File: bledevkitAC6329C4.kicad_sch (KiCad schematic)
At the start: 32 parts, among them J1 USB_C_Receptacle_USB2.0_16P, J2 Conn_01x02, J4 Conn_01x07, J5 Qwiic_I2C_connector, J6 Conn_01x07, J7 Conn_01x02, J8 Conn_01x01, SW1 SW_DPDT_x2, SW2 SW_DPDT_x2, SW3 SW_Push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

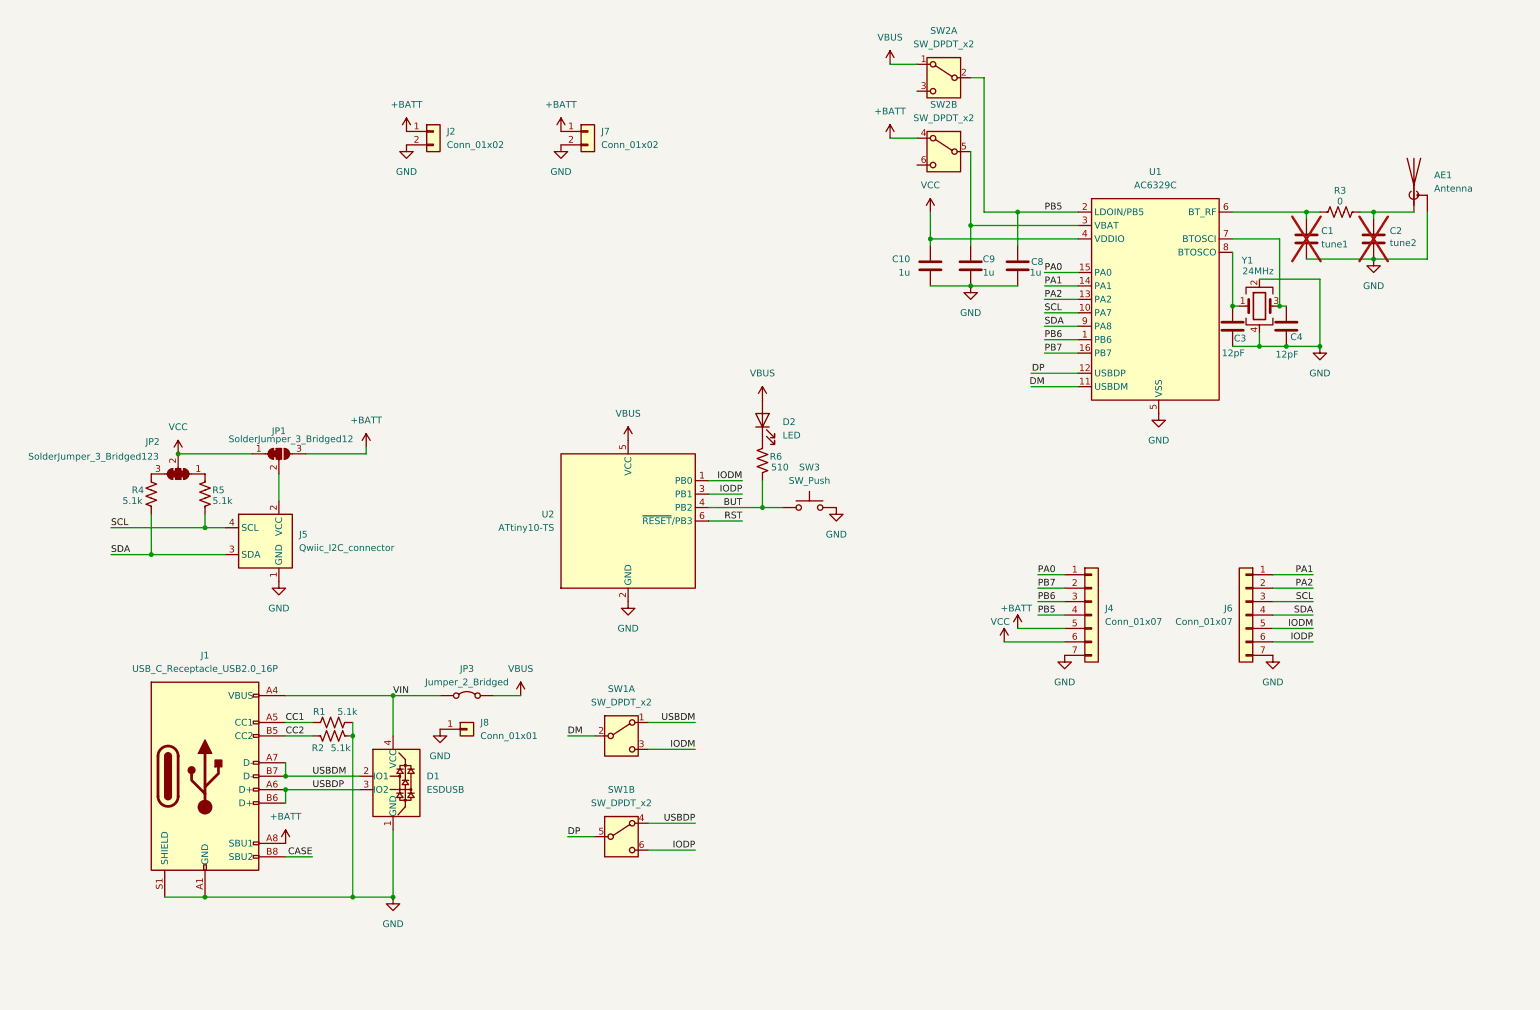
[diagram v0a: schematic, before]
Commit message: Finalized power topology
Isolated all power draws other than AC6329 behind current probe point.  Added auxiliary 3.3V regulator as an option for Qwiic header.  Shouldn't need any schematic changes, just on to making things fit and adding the switch footprints.
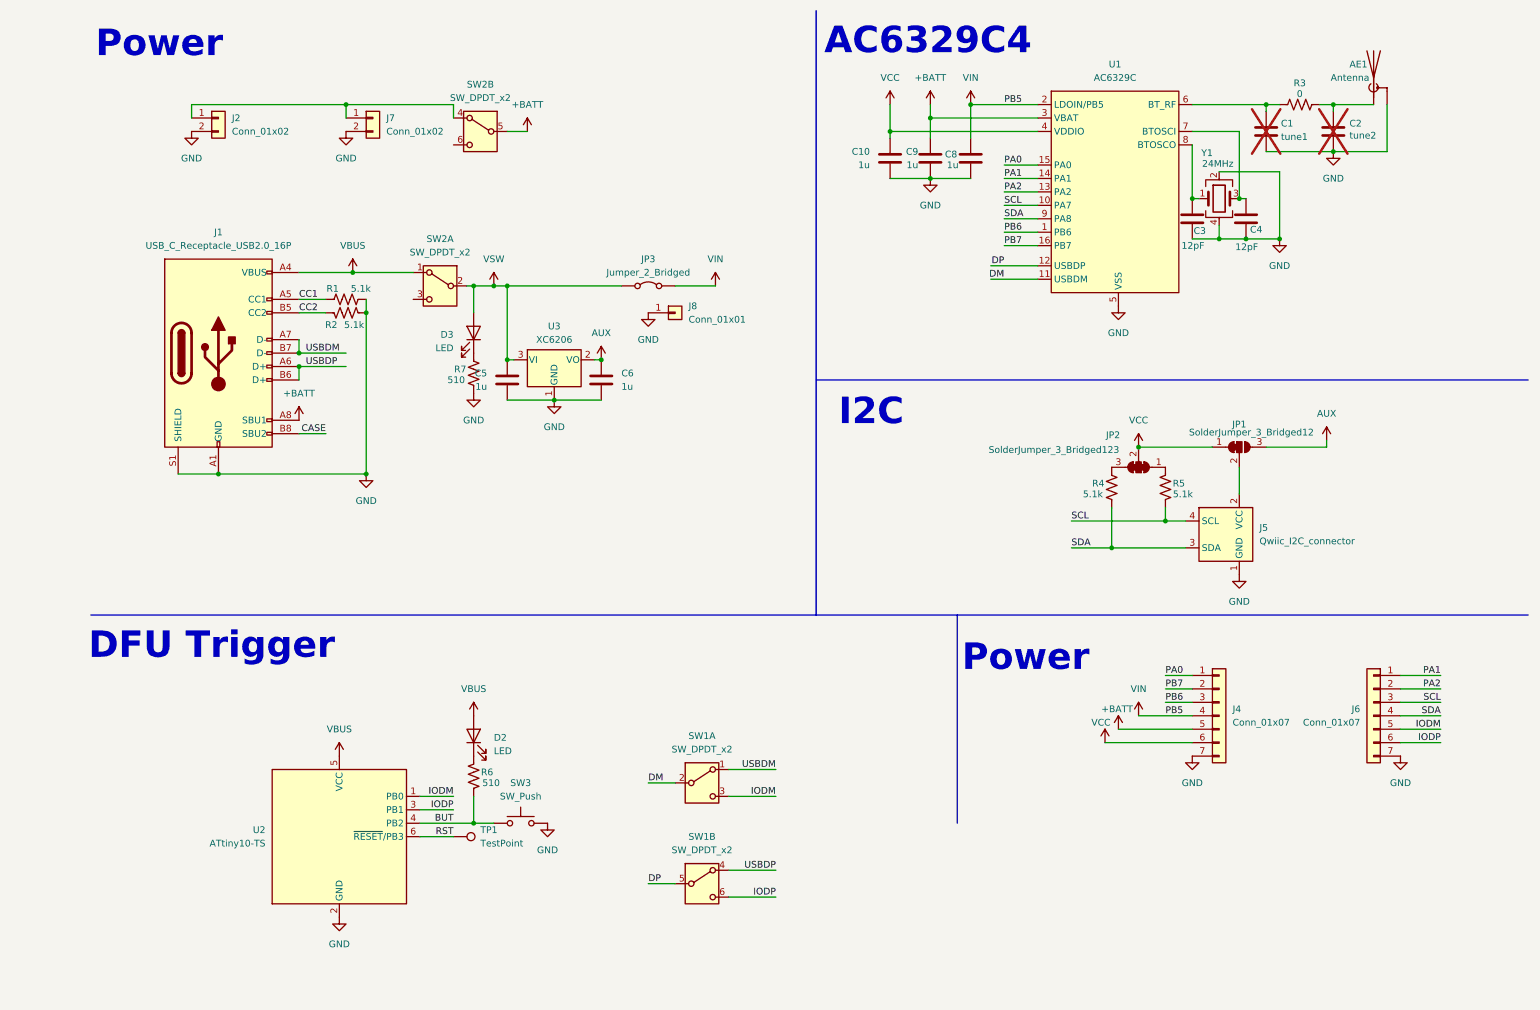
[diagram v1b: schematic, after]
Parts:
- removed D1: ESDUSB, Package_TO_SOT_SMD:SOT-143, symbol maxkicad:ESDUSB
- added C5, C6: 1u, Capacitor_SMD:C_0402_1005Metric, symbol Device:C
- added D3: LED, LED_SMD:LED_0402_1005Metric, symbol Device:LED
- added R7: 510, Resistor_SMD:R_0402_1005Metric, symbol Device:R_US
- added TP1: TestPoint, TestPoint:TestPoint_Pad_D3.0mm, symbol Connector:TestPoint
- added U3: XC6206, Package_TO_SOT_SMD:SOT-23-3, symbol Regulator_Linear:XC6206PxxxMR
- J5: footprint Connector_JST:JST_SH_BM04B-SRSS-TB_1x04-1MP_P1.00mm_Vertical -> Connector_JST:JST_SH_SM04B-SRSS-TB_1x04-1MP_P1.00mm_Horizontal
- J8: footprint Connector_PinSocket_2.54mm:PinSocket_1x01_P2.54mm_Vertical -> Connector_PinHeader_2.54mm:PinHeader_1x01_P2.54mm_Vertical
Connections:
- net +BATT: now also C9.1, SW2.5 (B), U1.3 (VBAT); no longer J2.1 (Pin_1), J7.1 (Pin_1), JP1.3 (B), SW2.4 (A)
- net GND: now also C5.2, C6.2, R7.1, U3.1 (GND)
- net RST: now also TP1.1
- net VBUS: now also J1.A4 (VBUS), J1.A9 (VBUS), J1.B4 (VBUS), J1.B9 (VBUS); no longer JP3.2 (B)
- net VIN: now also C8.1, J4.4 (Pin_4), JP3.2 (B), U1.2 (LDOIN/PB5); no longer J1.A4 (VBUS), J1.A9 (VBUS), J1.B4 (VBUS), J1.B9 (VBUS), JP3.1 (A)
- removed net PB5: C8.1, J4.4 (Pin_4), SW2.2 (B), U1.2 (LDOIN/PB5)
- new net: J2.1 (Pin_1), J7.1 (Pin_1), SW2.4 (A)
- new net: D3.1 (K), R7.2
- new net AUX: C6.1, JP1.3 (B), U3.2 (VO)
- new net VSW: C5.1, D3.2 (A), JP3.1 (A), SW2.2 (B), U3.3 (VI)
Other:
- note added: "AC6329C4"
- note added: "DFU Trigger"
- note added: "I2C"
- note added: "Power"
- moved on the sheet: AE1, C1, C10, C2, C3, C4, C8, C9, D2, J1, J2, J4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

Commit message: Finalized switches, chose modern DFU trigger
Switched to the newest series of the ATTINY line for UPDI programming, which can be done over the USB-C connector for simplicity of flashing.  Also made custom footprints for SMD DPDT slide switches.  Temp routing 80% done.
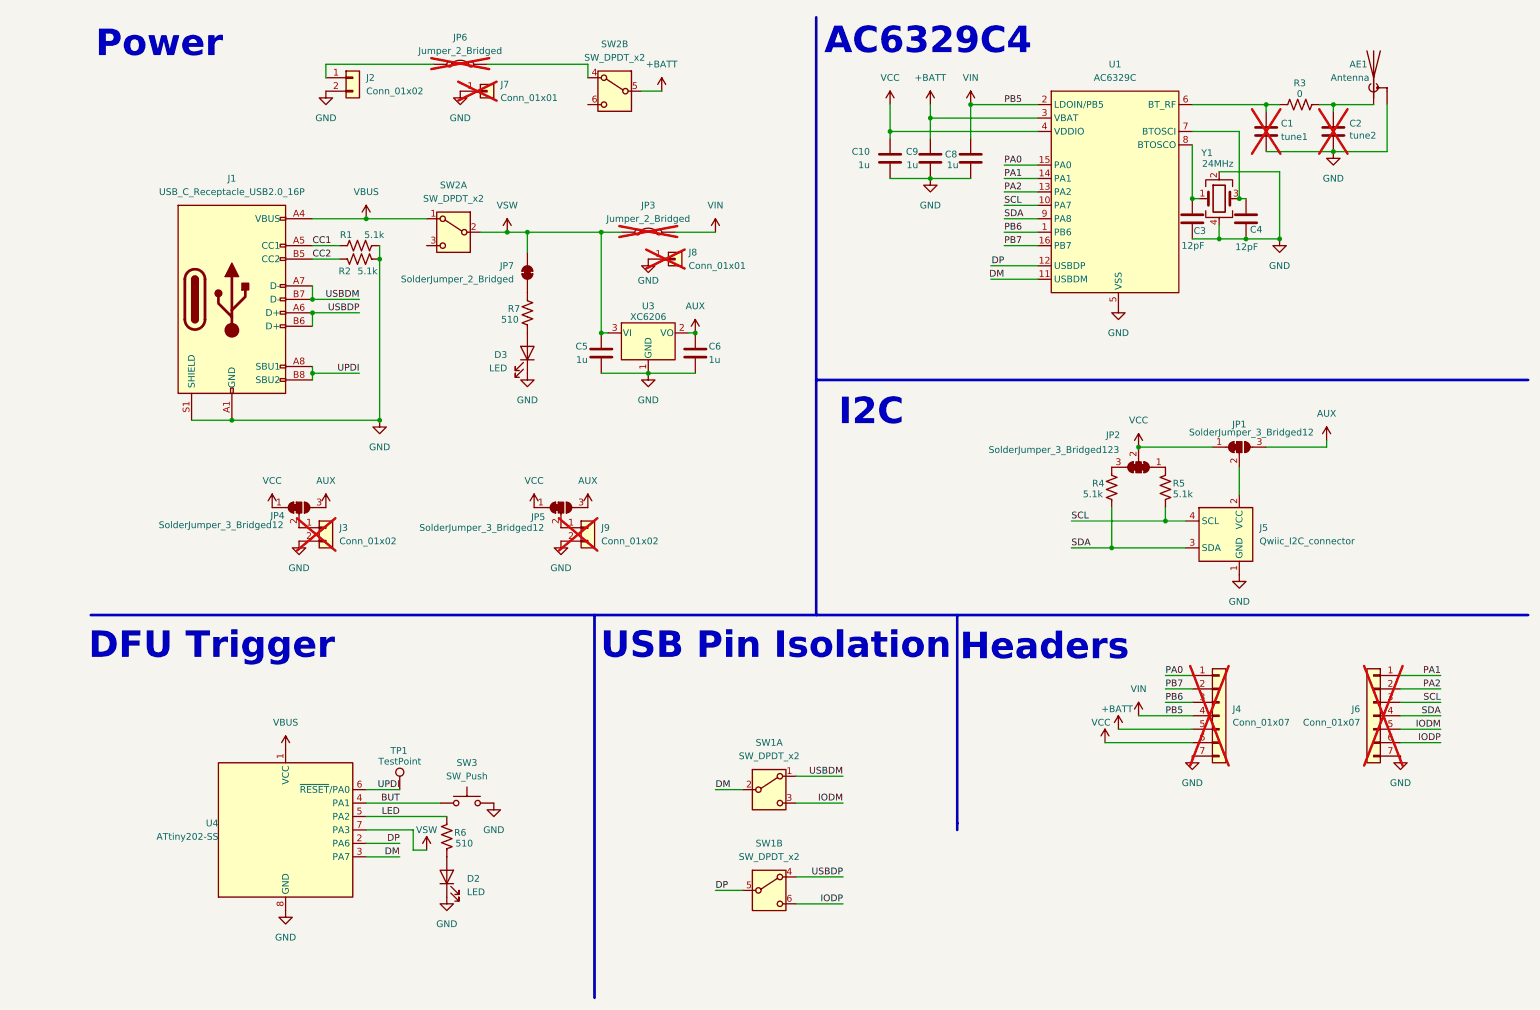
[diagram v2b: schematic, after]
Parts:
- removed J7: Conn_01x02, Connector_PinHeader_2.54mm:PinHeader_1x02_P2.54mm_Vertical, symbol Connector_Generic:Conn_01x02
- removed U2: ATtiny10-TS, Package_TO_SOT_SMD:SOT-23-6, symbol MCU_Microchip_ATtiny:ATtiny10-TS
- added J3, J9: Conn_01x02, Connector_PinHeader_2.54mm:PinHeader_1x02_P2.54mm_Vertical, symbol Connector_Generic:Conn_01x02
- added J7: Conn_01x01, Connector_PinHeader_2.54mm:PinHeader_1x01_P2.54mm_Vertical, symbol Connector_Generic:Conn_01x01
- added JP4, JP5: SolderJumper_3_Bridged12, Jumper:SolderJumper-3_P1.3mm_Bridged12_RoundedPad1.0x1.5mm, symbol Jumper:SolderJumper_3_Bridged12
- added JP6: Jumper_2_Bridged, Connector_PinHeader_2.54mm:PinHeader_1x02_P2.54mm_Vertical, symbol Jumper:Jumper_2_Bridged
- added JP7: SolderJumper_2_Bridged, Jumper:SolderJumper-2_P1.3mm_Bridged_RoundedPad1.0x1.5mm, symbol Jumper:SolderJumper_2_Bridged
- added U4: ATtiny202-SS, Package_SO:SOIC-8_3.9x4.9mm_P1.27mm, symbol MCU_Microchip_ATtiny:ATtiny202-SS
- J4, J6, J8, JP3: now not fitted
- SW1, SW2: footprint Button_Switch_SMD:SW_DPDT_CK_JS202011JCQN -> maxfootprints:DPDT-Slide_top; LCSC (none) -> C2837066
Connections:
- net RST is gone; now on net UPDI: TP1.1
- net +BATT: no longer J1.A8 (SBU1)
- net AUX: now also JP4.3 (B), JP5.3 (B)
- net BUT: now also U4.4 (PA1); no longer R6.1
- net DM: now also U4.3 (PA7)
- net DP: now also U4.2 (PA6)
- net GND: now also D2.1 (K), D3.1 (K), J3.2 (Pin_2), J7.1 (Pin_1), J9.2 (Pin_2), U4.8 (GND); no longer R7.1
- net VBUS: now also U4.1 (VCC); no longer D2.2 (A)
- net VCC: now also JP4.1 (A), JP5.1 (A)
- net VSW: now also JP7.1 (A), U4.7 (PA3); no longer D3.2 (A)
- net LED: now reaches R6.2
- net LED: now also U4.5 (PA2); no longer D2.1 (K)
- net at SW2.4 (A): now also JP6.2 (B); no longer J2.1 (Pin_1)
- net at R7.2: now also JP7.2 (B); no longer D3.1 (K)
- net CASE renamed UPDI
- net UPDI: now also J1.A8 (SBU1), U4.6 (~{RESET}/PA0)
- new net: D2.2 (A), R6.1
- new net: J9.1 (Pin_1), JP5.2 (C)
- new net: D3.2 (A), R7.1
- new net: J3.1 (Pin_1), JP4.2 (C)
- new net: J2.1 (Pin_1), JP6.1 (A)
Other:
- note added: "Headers"
- note added: "USB Pin Isolation"
- moved on the sheet: C5, C6, D2, D3, J1, J2, R1, R2, R6, R7, SW1A, SW1B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

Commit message: Finished routing
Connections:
- net +BATT: now also JP6.2 (B); no longer SW2.5 (B)
- net EXT: now reaches SW2.4 (A)
- net EXT: now also J2.1 (Pin_1); no longer JP6.2 (B)
- net at JP6.1 (A): now also SW2.5 (B); no longer J2.1 (Pin_1)
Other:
- moved on the sheet: J7, JP6, SW2B
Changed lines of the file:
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@@
 	(wire
 		(pts
+			(xy 57.15 21.59) (xy 77.47 21.59)
+		)
+		(stroke
+			(width 0)
+			(type default)
+		)
+	)
+	(wire
+		(pts
 			(xy 54.61 80.01) (xy 63.5 80.01)
 		)
@@
 		)
 	)
-	(wire
-		(pts
-			(xy 77.47 21.59) (xy 57.15 21.59)
-		)
-		(stroke
-			(width 0)
-			(type default)
-		)
-	)
 	(polyline
 		(pts
@@
 	(wire
 		(pts
-			(xy 106.68 24.13) (xy 106.68 21.59)
+			(xy 73.66 166.37) (xy 64.77 166.37)
 		)
 		(stroke
@@
 	(wire
 		(pts
-			(xy 73.66 166.37) (xy 64.77 166.37)
+			(xy 109.22 72.39) (xy 110.49 72.39)
 		)
 		(stroke
@@
 	(wire
 		(pts
-			(xy 109.22 72.39) (xy 110.49 72.39)
+			(xy 185.42 40.64) (xy 191.77 40.64)
 		)
 		(stroke
@@
 	(wire
 		(pts
-			(xy 185.42 40.64) (xy 191.77 40.64)
+			(xy 87.63 22.86) (xy 87.63 21.59)
 		)
 		(stroke
@@
 	(wire
 		(pts
+			(xy 87.63 21.59) (xy 93.98 21.59)
+		)
+		(stroke
+			(width 0)
+			(type default)
+		)
+	)
+	(wire
+		(pts
 			(xy 205.74 113.03) (xy 219.71 113.03)
 		)
@@
 	(wire
 		(pts
+			(xy 77.47 20.32) (xy 77.47 21.59)
+		)
+		(stroke
+			(width 0)
+			(type default)
+		)
+	)
+	(wire
+		(pts
 			(xy 215.9 105.41) (xy 215.9 107.95)
 		)
@@
 	(wire
 		(pts
+			(xy 104.14 21.59) (xy 115.57 21.59)
+		)
+		(stroke
+			(width 0)
+			(type default)
+		)
+	)
+	(wire
+		(pts
 			(xy 64.77 161.29) (xy 78.74 161.29)
 		)
@@
 	(wire
 		(pts
-			(xy 87.63 21.59) (xy 106.68 21.59)
-		)
-		(stroke
-			(width 0)
-			(type default)
-		)
-	)
-	(wire
-		(pts
 			(xy 57.15 21.59) (xy 57.15 24.13)
 		)
@@
 	(wire
 		(pts
-			(xy 116.84 26.67) (xy 120.65 26.67)
-		)
-		(stroke
-			(width 0)
-			(type default)
-		)
-	)
-	(wire
-		(pts
 			(xy 95.25 53.34) (xy 109.22 53.34)
 		)
@@
 		)
 	)
+	(label "EXT"
+		(at 58.42 21.59 0)
+		(fields_autoplaced yes)
+		(effects
+			(font
+				(size 1.27 1.27)
+			)
+			(justify left bottom)
+		)
+	)
 	(label "DP"
 		(at 185.42 59.69 180)
@@
 	(symbol
 		(lib_id "power:+BATT")
-		(at 120.65 26.67 0)
+		(at 115.57 21.59 0)
 		(unit 1)
 		(exclude_from_sim no)
@@
 		(fields_autoplaced yes)
 		(property "Reference" "#PWR031"
-			(at 120.65 30.48 0)
+			(at 115.57 25.4 0)
 			(effects
 				(font
@@
 		)
 		(property "Value" "+BATT"
-			(at 120.65 21.59 0)
+			(at 115.57 16.51 0)
 			(effects
 				(font
@@
 		)
 		(property "Footprint" ""
-			(at 120.65 26.67 0)
+			(at 115.57 21.59 0)
 			(effects
 				(font
@@
 		)
 		(property "Datasheet" ""
-			(at 120.65 26.67 0)
+			(at 115.57 21.59 0)
 			(effects
 				(font
@@
 		)
 		(property "Description" "Power symbol creates a global label with name \"+BATT\""
-			(at 120.65 26.67 0)
+			(at 115.57 21.59 0)
 			(effects
 				(font
@@
 	(symbol
 		(lib_id "Connector_Generic:Conn_01x01")
-		(at 87.63 26.67 0)
+		(at 104.14 26.67 0)
 		(unit 1)
 		(exclude_from_sim no)
@@
 		(fields_autoplaced yes)
 		(property "Reference" "J7"
-			(at 90.17 25.3999 0)
+			(at 106.68 25.3999 0)
 			(effects
 				(font
@@
 		)
 		(property "Value" "Conn_01x01"
-			(at 90.17 27.9399 0)
+			(at 106.68 27.9399 0)
 			(effects
 				(font
@@
 		)
 		(property "Footprint" "Connector_PinHeader_2.54mm:PinHeader_1x01_P2.54mm_Vertical"
-			(at 87.63 26.67 0)
+			(at 104.14 26.67 0)
 			(effects
 				(font
@@
 		)
 		(property "Datasheet" "~"
-			(at 87.63 26.67 0)
+			(at 104.14 26.67 0)
 			(effects
 				(font
@@
 		)
 		(property "Description" "Generic connector, single row, 01x01, script generated (kicad-library-utils/schlib/autogen/connector/)"
-			(at 87.63 26.67 0)
+			(at 104.14 26.67 0)
 			(effects
 				(font
@@
 	(symbol
 		(lib_id "Switch:SW_DPDT_x2")
-		(at 111.76 26.67 0)
+		(at 82.55 22.86 0)
 		(mirror y)
 		(unit 2)
@@
 		(dnp no)
 		(property "Reference" "SW2"
-			(at 111.76 17.78 0)
+			(at 82.55 13.97 0)
 			(effects
 				(font
@@
 		)
 		(property "Value" "SW_DPDT_x2"
-			(at 111.76 20.32 0)
+			(at 82.55 16.51 0)
 			(effects
 				(font
@@
 		)
 		(property "Footprint" "maxfootprints:DPDT-Slide_top"
-			(at 111.76 26.67 0)
+			(at 82.55 22.86 0)
 			(effects
 				(font
@@
 		)
 		(property "Datasheet" "~"
-			(at 111.76 26.67 0)
+			(at 82.55 22.86 0)
 			(effects
 				(font
@@
 		)
 		(property "Description" "Switch, dual pole double throw, separate symbols"
-			(at 111.76 26.67 0)
+			(at 82.55 22.86 0)
 			(effects
 				(font
@@
 		)
 		(property "LCSC" "C2837066"
-			(at 111.76 26.67 0)
+			(at 82.55 22.86 0)
 			(effects
 				(font
@@
 	(symbol
 		(lib_id "Jumper:Jumper_2_Bridged")
-		(at 82.55 21.59 0)
+		(at 99.06 21.59 0)
 		(unit 1)
 		(exclude_from_sim yes)
@@
 		(dnp yes)
 		(property "Reference" "JP6"
-			(at 82.55 16.51 0)
+			(at 99.06 16.51 0)
 			(effects
 				(font
@@
 		)
 		(property "Value" "Jumper_2_Bridged"
-			(at 82.55 19.05 0)
+			(at 99.06 19.05 0)
 			(effects
 				(font
@@
 		)
 		(property "Footprint" "Connector_PinHeader_2.54mm:PinHeader_1x02_P2.54mm_Vertical"
-			(at 82.55 21.59 0)
+			(at 99.06 21.59 0)
 			(effects
 				(font
@@
 		)
 		(property "Datasheet" "~"
-			(at 82.55 21.59 0)
+			(at 99.06 21.59 0)
 			(effects
 				(font
@@
 		)
 		(property "Description" "Jumper, 2-pole, closed/bridged"
-			(at 82.55 21.59 0)
+			(at 99.06 21.59 0)
 			(effects
 				(font
@@
 	(symbol
 		(lib_id "power:GND")
-		(at 82.55 26.67 0)
+		(at 99.06 26.67 0)
 		(unit 1)
 		(exclude_from_sim no)
@@
 		(fields_autoplaced yes)
 		(property "Reference" "#PWR024"
-			(at 82.55 33.02 0)
+			(at 99.06 33.02 0)
 			(effects
 				(font
@@
 		)
 		(property "Value" "GND"
-			(at 82.55 31.75 0)
+			(at 99.06 31.75 0)
 			(effects
 				(font
@@
 		)
 		(property "Footprint" ""
-			(at 82.55 26.67 0)
+			(at 99.06 26.67 0)
 			(effects
 				(font
@@
 		)
 		(property "Datasheet" ""
-			(at 82.55 26.67 0)
+			(at 99.06 26.67 0)
 			(effects
 				(font
@@
 		)
 		(property "Description" "Power symbol creates a global label with name \"GND\" , ground"
-			(at 82.55 26.67 0)
+			(at 99.06 26.67 0)
 			(effects
 				(font
